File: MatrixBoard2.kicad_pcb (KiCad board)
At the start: 2 copper layers, 70 x 60 mm, 204 parts, among them J1 Conn_01x03_Male, J2 Conn_01x03_Male

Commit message: Now with MOAR 3D
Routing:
- net Net-(D1-Pad3): track 23.8 -> 22.7 mm
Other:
- board text added: "${TITLE} (v${REVISION})"
- board text removed: "12x8 RGB Matrix (v0.0.1)"

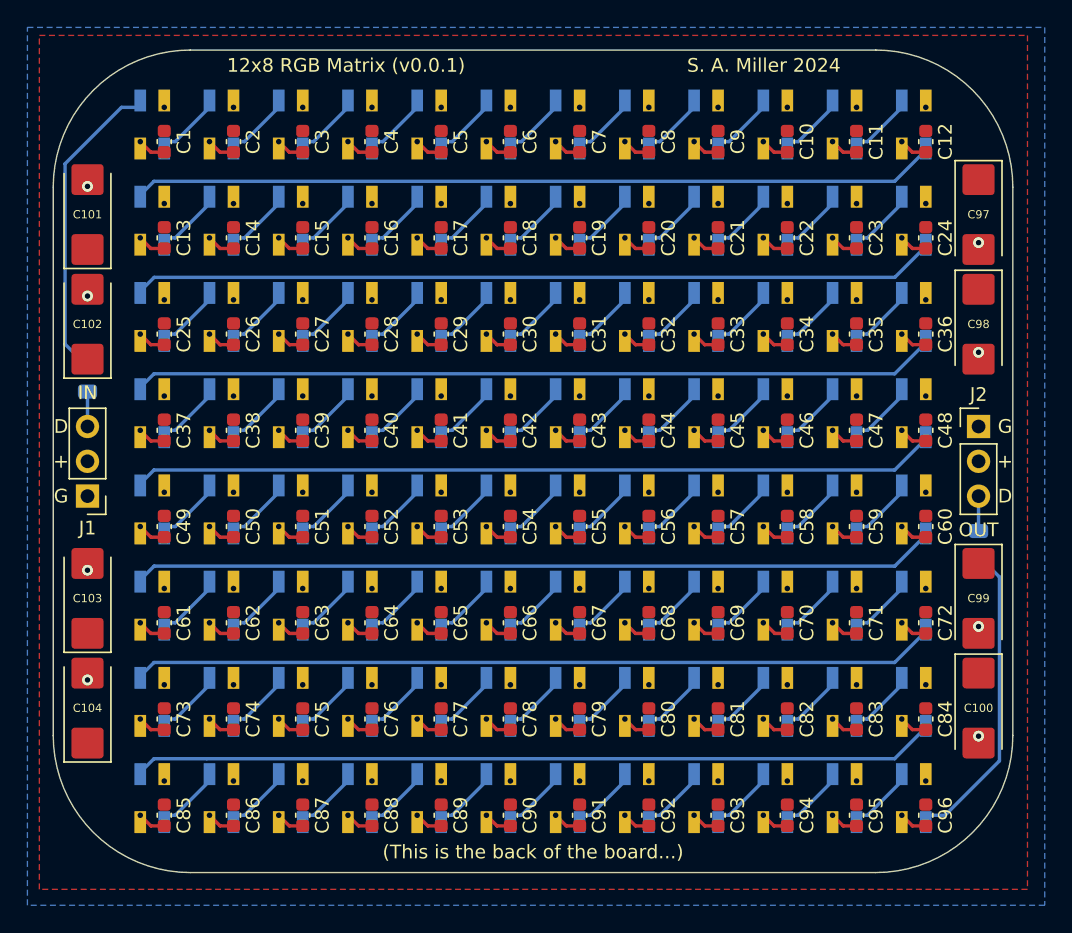
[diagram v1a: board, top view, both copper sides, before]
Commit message: A bunch of cosmetic changes... (Mostly silkscreen OCD)
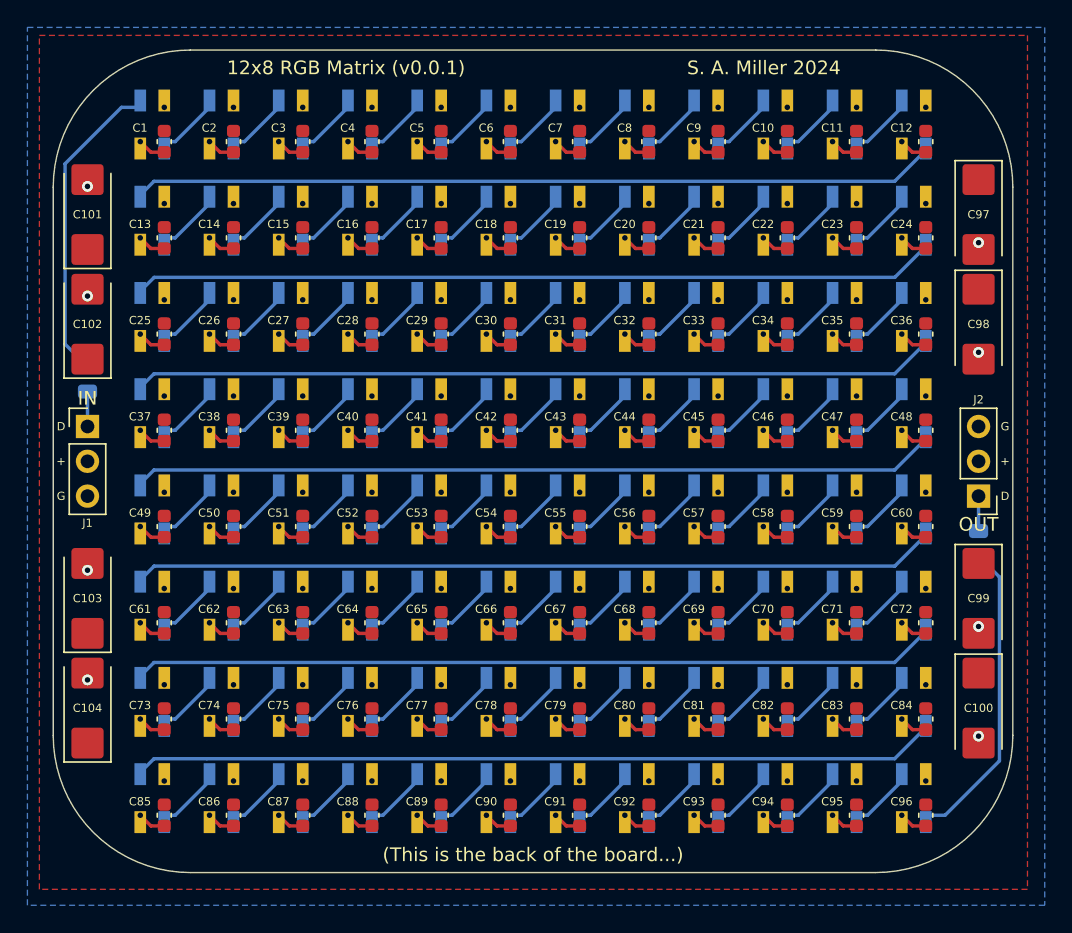
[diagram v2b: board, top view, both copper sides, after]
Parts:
- moved J1 5.08 mm to (67.5, 97.5), turned to 0 degrees
- moved J2 5.08 mm to (132.5, 102.5), turned to 180 degrees
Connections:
- J1 pad 1: GND -> Net-(J1-Pad1)
- J1 pad 3: Net-(J1-Pad3) -> GND
- J2 pad 1: GND -> Net-(J2-Pad1)
- J2 pad 3: Net-(J2-Pad3) -> GND
- R1 pad 2: Net-(J1-Pad3) -> Net-(J1-Pad1)
- R2 pad 2: Net-(J2-Pad3) -> Net-(J2-Pad1)
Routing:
- net Net-(J2-Pad3): track 2.55 -> 0.00 mm
- net Net-(J2-Pad1): track 0.00 -> 2.55 mm
- net Net-(J1-Pad3): track 2.55 -> 0.00 mm
- net Net-(J1-Pad1): track 0.00 -> 2.55 mm

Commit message: Added the rabbit back in...
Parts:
- added REF**: DagNabbit, tightstuff:DagNabbit, B.Cu at (132.3, 119.2)
